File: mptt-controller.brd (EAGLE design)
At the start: 78.4 x 50.8 mm, 60 parts, among them IC1 ATSAMD09D14A-MU, Q1 MMBTA56LT1G, Q5 CSD18533KCS, Q6 CSD18533KCS, U1 AP2112K, U2 LM5109BMA/NOPB

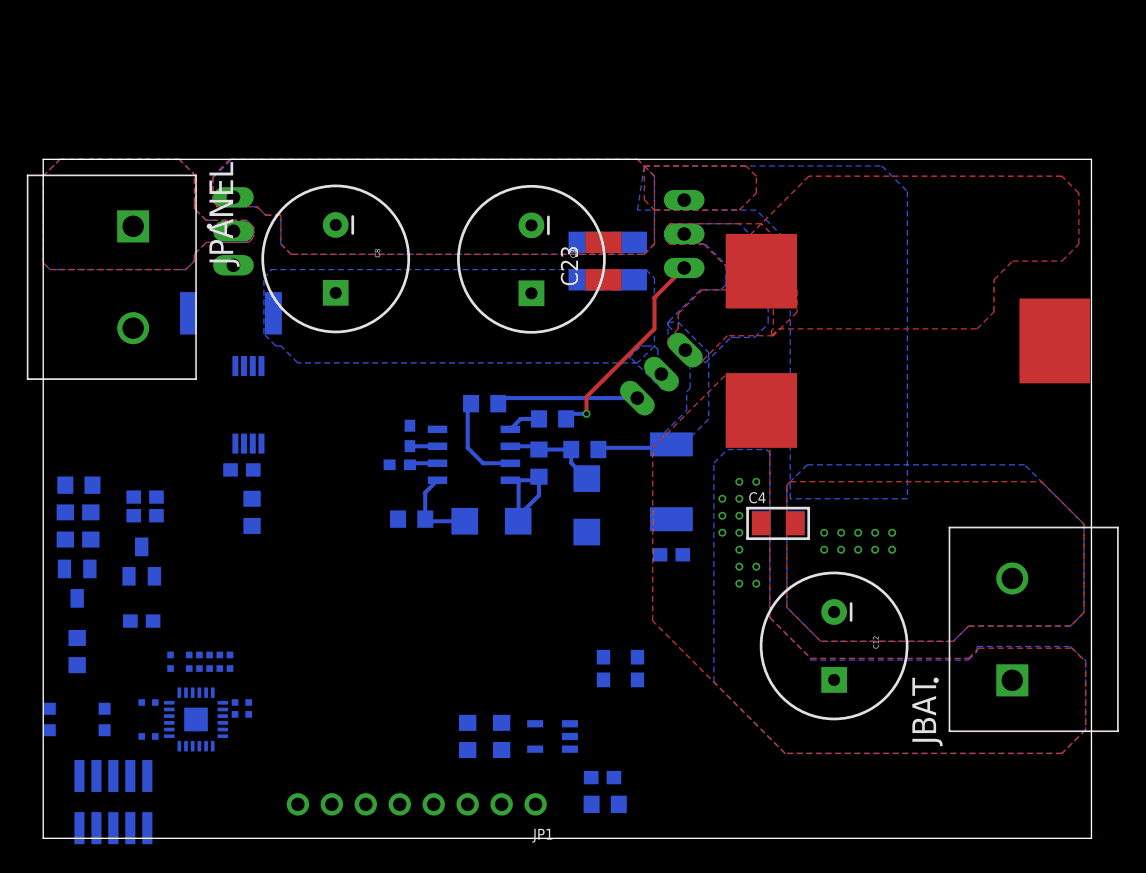
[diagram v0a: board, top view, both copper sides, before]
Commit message: Checkpoint - More Vias and polygonal planes.
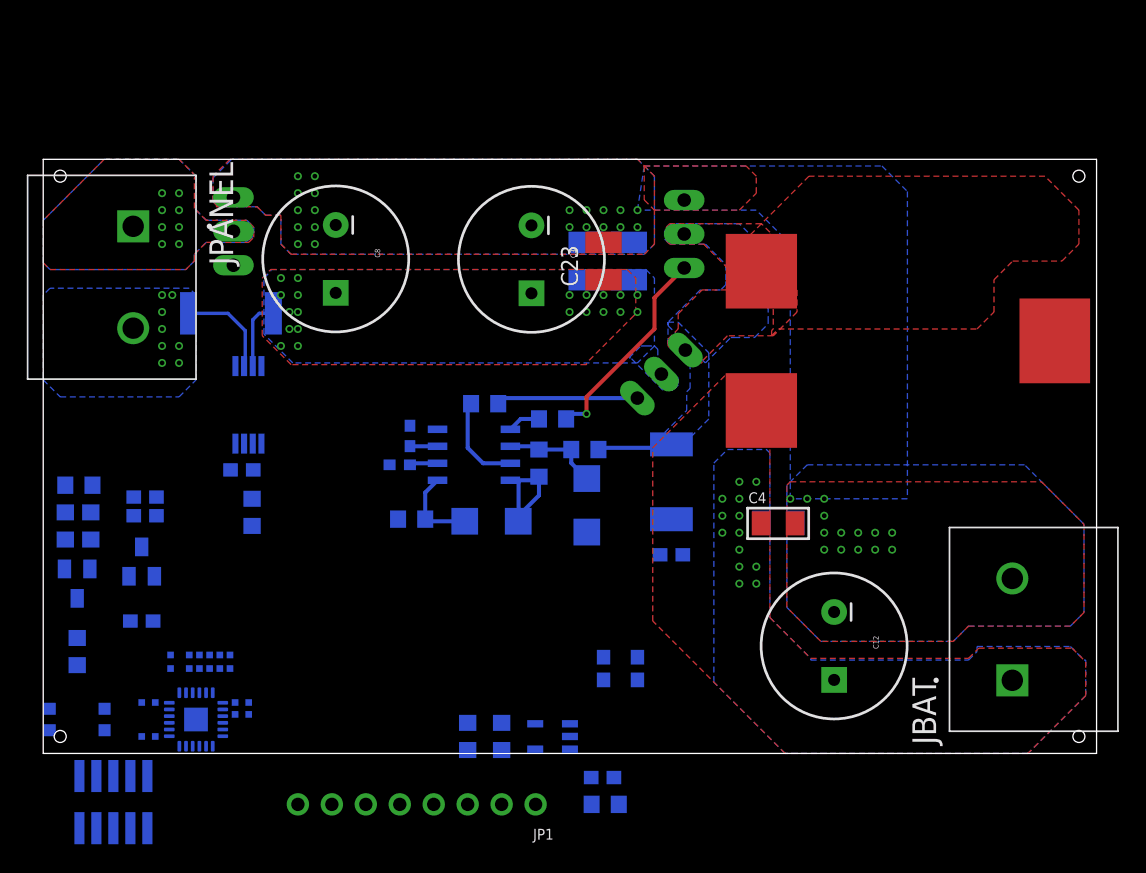
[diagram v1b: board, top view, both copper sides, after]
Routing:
- net P+: track 0.00 -> 6.81 mm, vias 0 -> 8
- net V_IN: track 0.00 -> 5.21 mm, vias 0 -> 20
- added copper zone on layer 16, net P+
- added copper zone on layer 1, net V_IN
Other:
- board size 78.4 x 50.8 mm -> 78.8 x 44.4 mm

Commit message: Very close to being finished.
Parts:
- moved SW1 13.4 mm to (14.9, 16.4), turned to 270 degrees
- moved C13 12.1 mm to (21.1, 19.6), turned to 90 degrees
- moved C14 12.0 mm to (23.9, 19.6)
- moved R16 12.0 mm to (24.6, 19.6)
- moved R20 12.0 mm to (26.3, 16.5)
- moved C11 12.0 mm to (22.4, 19.6)
- moved C16 12.0 mm to (19.3, 16.5)
- moved IC1 12.0 mm to (22.9, 15.2)
- moved R15 12.0 mm to (23.1, 19.6)
- moved R18 12.0 mm to (26.3, 15.6)
- moved R19 12.0 mm to (19.3, 14.0)
- moved R3 12.0 mm to (25.4, 19.6)
- moved X1 8.88 mm to (11.0, 10.4), turned to 0 degrees
- moved R14 8.08 mm to (7.87, 21.0), turned to 180 degrees
- moved Q1 7.65 mm to (7.87, 25.5), turned to 0 degrees
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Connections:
- net N$8 renamed VS
- new net N$3: IC1.8, R18.1
- net GND: now also JP1.8
- net P_EN: no longer IC1.8, R18.1
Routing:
- net GND: track 0.00 -> 61.0 mm, vias 34 -> 54
- net VCC_3V3: track 0.00 -> 38.6 mm
- net VCC_10V: track 6.31 -> 37.4 mm
- net P_V: track 0.00 -> 21.3 mm, vias 0 -> 4
- net BAT_V: track 0.00 -> 17.8 mm, vias 0 -> 2
- net P-: track 0.00 -> 17.7 mm, vias 8 -> 10
- net P_EN: track 0.00 -> 17.4 mm, vias 0 -> 2
- net N$2: track 0.00 -> 16.2 mm, vias 0 -> 1
- net P_I: track 0.00 -> 15.7 mm, vias 0 -> 2
- net P+: track 6.81 -> 22.2 mm
- net LI: track 2.07 -> 15.8 mm, vias 0 -> 2
- net SWCLK: track 0.00 -> 11.2 mm, vias 0 -> 2
- net HI: track 2.11 -> 12.6 mm, vias 0 -> 2
- net BUCK_OUT: track 0.00 -> 10.3 mm
- net SWDIO: track 0.00 -> 8.32 mm, vias 0 -> 2
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
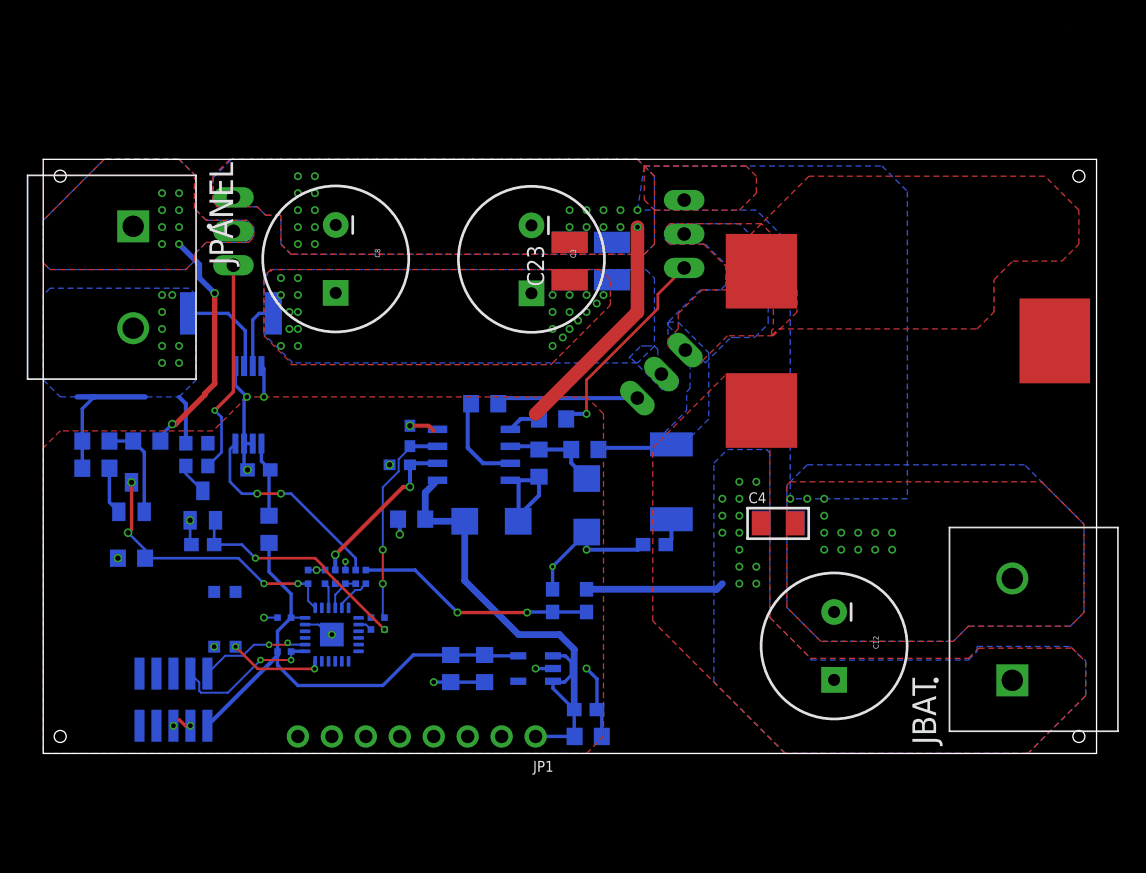
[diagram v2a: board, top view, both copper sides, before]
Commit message: Board documentation layer and add a cap for VREFA.
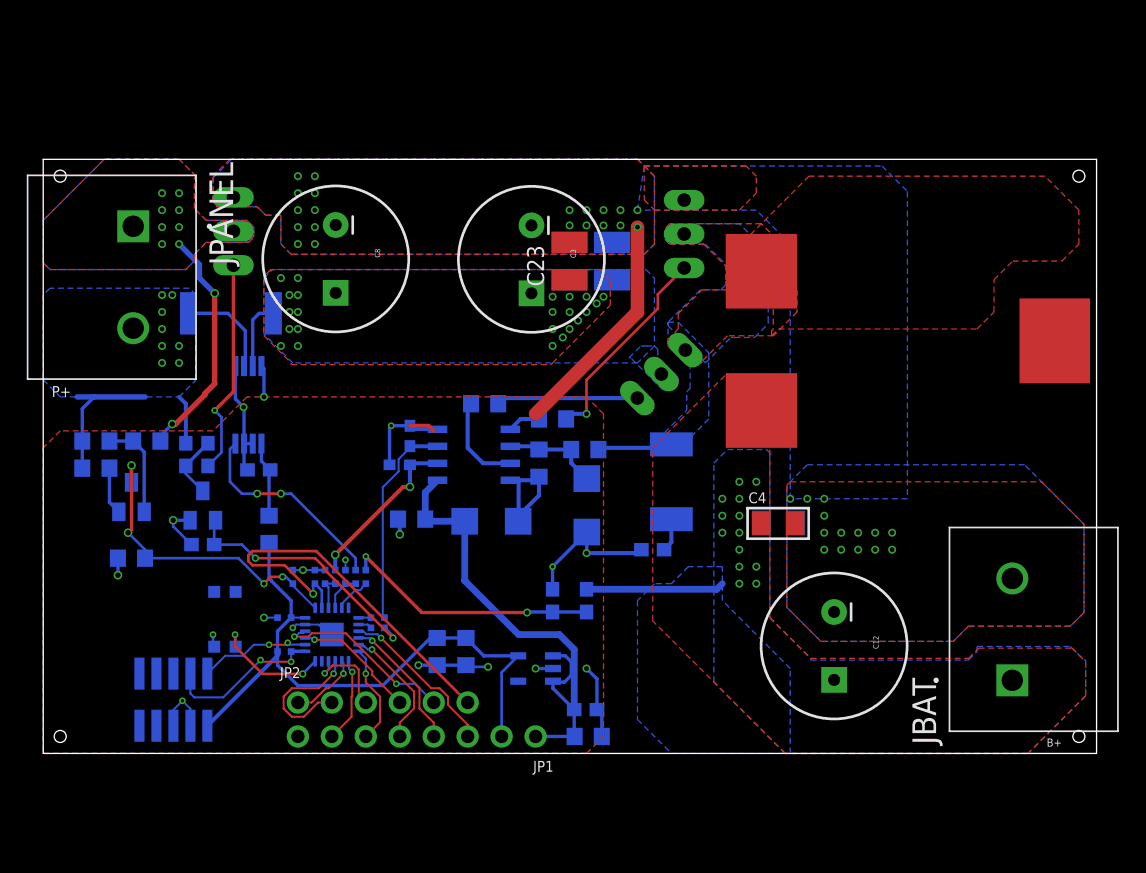
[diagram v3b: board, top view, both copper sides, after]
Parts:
- added C17: 0.1uF, ATSAMD09D14 Breakout rev B:_0402MP
- added JP2: (no value), Adafruit Metro M0 Express:1X06_ROUND
- moved C5 1.89 mm to (32.9, 14.0)
- moved C2 1.63 mm to (30.7, 14.0)
- moved C13 1.14 mm to (19.9, 19.6)
- moved CSNUB 0.40 mm to (46.9, 21.6)
- moved R18 0.13 mm to (26.3, 15.7)
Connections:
- new net AREF: C17.1, IC1.2, JP2.6
- new net PA10: IC1.9, JP1.3
- new net PA11: IC1.10, JP1.4
- new net PA14: IC1.11, JP1.5
- new net PA15: IC1.12, JP1.6
- new net PA16: IC1.13, JP1.7
- new net PA17: IC1.14, JP2.1
- new net PA22: IC1.15, JP2.2
- new net PA23: IC1.16, JP2.3
- new net PA24: IC1.21, JP2.4
- new net PA25: IC1.22, JP2.5
- net GND: now also C17.2
- net VCC_3V3: now also JP1.2
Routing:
- net AREF: track 0.00 -> 30.4 mm, vias 0 -> 1
- net GND: track 61.0 -> 80.1 mm, vias 54 -> 52
- net PA25: track 0.00 -> 13.7 mm, vias 0 -> 2
- net PA10: track 0.00 -> 12.3 mm, vias 0 -> 1
- net PA22: track 0.00 -> 10.6 mm, vias 0 -> 1
- net PA11: track 0.00 -> 10.2 mm, vias 0 -> 1
- net PA14: track 0.00 -> 9.40 mm, vias 0 -> 1
- net PA24: track 0.00 -> 9.26 mm, vias 0 -> 1
- net VCC_3V3: track 38.6 -> 46.2 mm
- net PA15: track 0.00 -> 7.48 mm, vias 0 -> 1
- net PA23: track 0.00 -> 6.62 mm, vias 0 -> 1
- net PA16: track 0.00 -> 6.36 mm, vias 0 -> 1
- net PA17: track 0.00 -> 5.27 mm, vias 0 -> 1
- net N$9: track 2.39 -> 4.77 mm
- net P_V: track 21.3 -> 23.6 mm
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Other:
- board text added: "10V"
- board text added: "3V3"
- board text added: "B+"
- board text added: "GND"
- board text added: "P+"
- board text added: "PA10"
- board text added: "PA11"
- board text added: "PA14"
- board text added: "PA15"
- board text added: "PA16"
- board text added: "PA17"
- board text added: "PA22"
- board text added: "PA23"
- board text added: "PA24"
- board text added: "PA25"
- board text added: "PA27"
